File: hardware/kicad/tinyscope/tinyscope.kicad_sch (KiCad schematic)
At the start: 0 parts

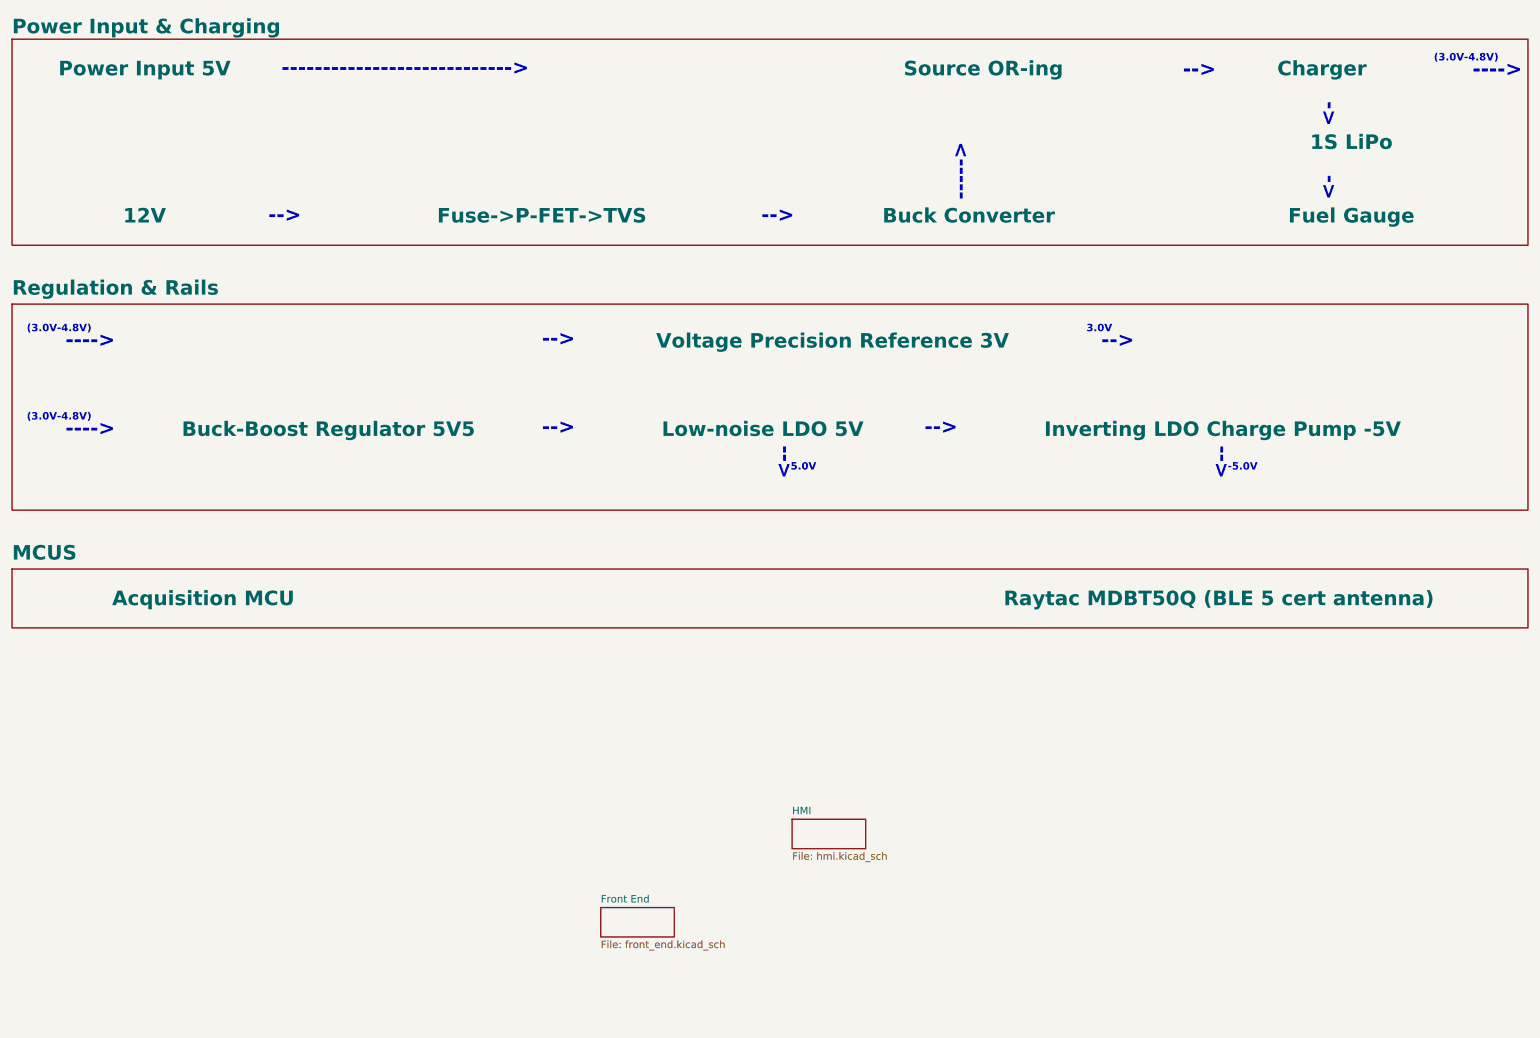
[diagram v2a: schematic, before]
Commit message: feat: hardware: Add tinyscope kicad project. Divide MCU schematic into acquisition and wireless parts
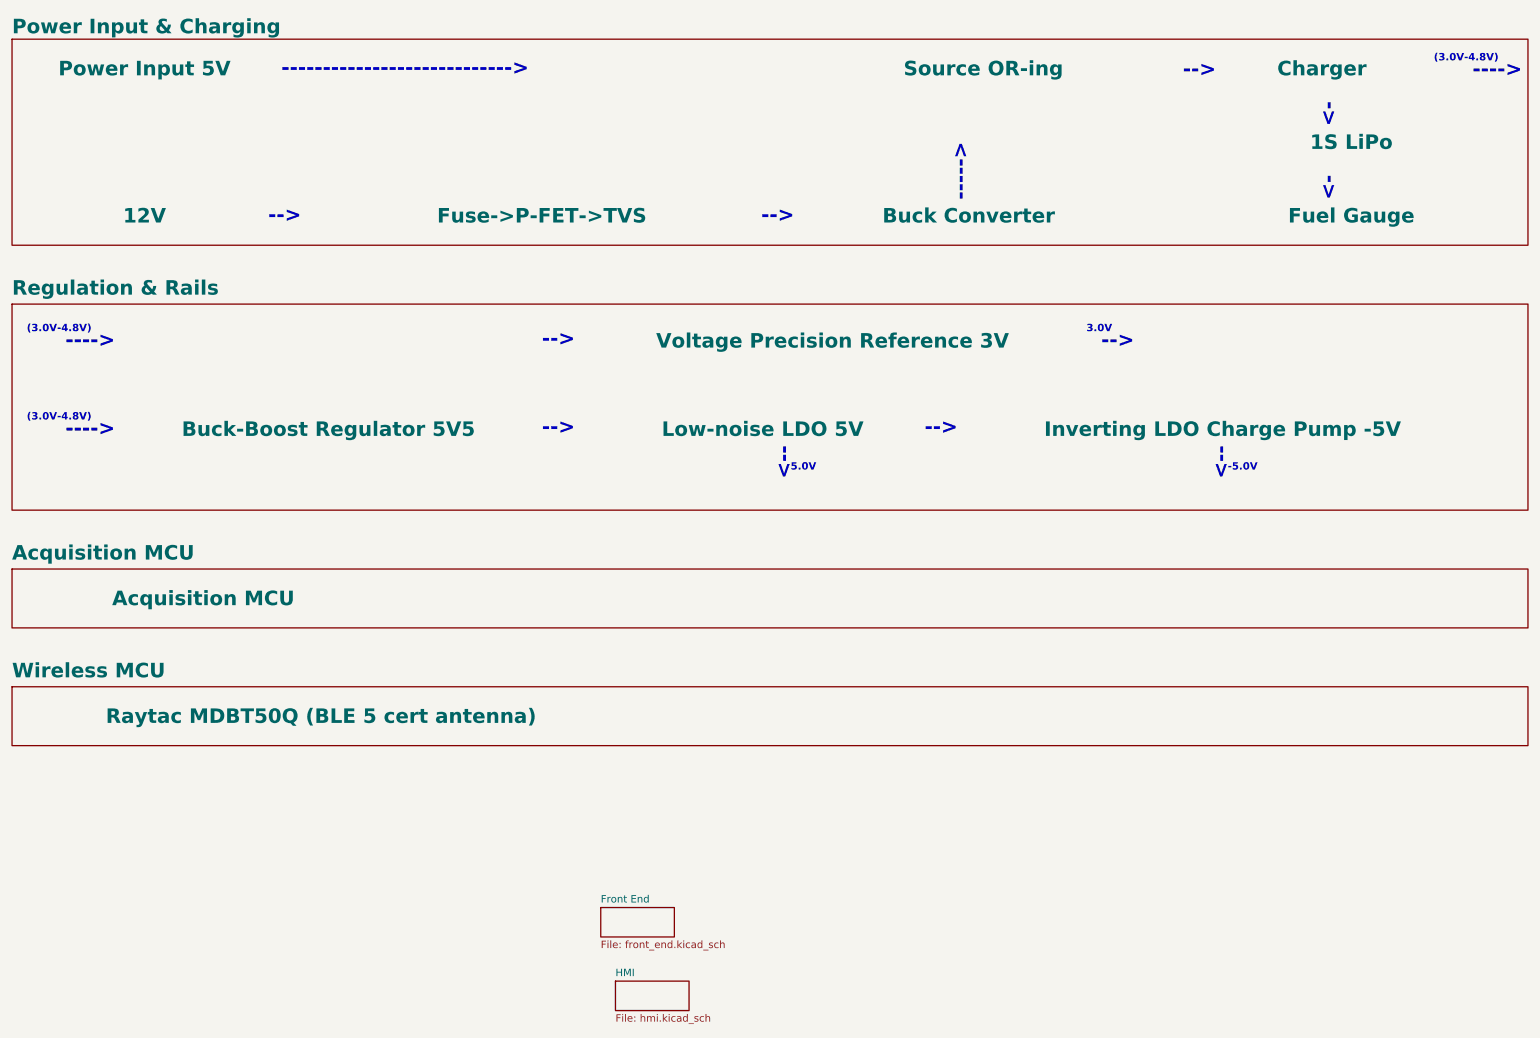
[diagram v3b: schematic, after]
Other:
- sheet MCUS renamed Acquisition MCU
- added sheet Wireless MCU (mcu_wireless.kicad_sch)
- sheet Acquisition MCU: file mcus.kicad_sch -> mcus_acquisition.kicad_sch
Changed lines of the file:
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@@
     )
   )
-  (sheet (at 152.4 154.94) (size 12.7 5.08) (fields_autoplaced)
+  (sheet (at 17.78 132.08) (size 261.62 10.16)
     (stroke (width 0.1524) (type solid))
     (fill (color 255 255 194 1.0000))
-    (property "Sheetname" "HMI" (at 152.4 154.2284 0)
+    (property "Sheetname" "Wireless MCU" (at 17.78 130.7534 0)
+      (effects (font (size 2.5 2.5) bold) (justify left bottom))
+    )
+    (property "Sheetfile" "mcu_wireless.kicad_sch" (at 17.78 142.8246 0)
+      (effects (font (size 1.27 1.27)) (justify left top) hide)
+    )
+    (property "nRF52840" "Raytac MDBT50Q (BLE 5 cert antenna)" (at 71.12 137.16 0) (show_name)
+      (effects (font (size 2.5 2.5) bold))
+    )
+    (instances
+      (project "tinyscope"
+        (path "/bb072e32-cc57-415a-8554-0e84d374f333" (page "7"))
+      )
+    )
+  )
+  (sheet (at 121.92 182.88) (size 12.7 5.08) (fields_autoplaced)
+    (stroke (width 0.1524) (type solid))
+    (fill (color 255 255 194 1.0000))
+    (property "Sheetname" "HMI" (at 121.92 182.1684 0)
       (effects (font (size 1.27 1.27)) (justify left bottom))
     )
-    (property "Sheetfile" "hmi.kicad_sch" (at 152.4 160.6046 0)
+    (property "Sheetfile" "hmi.kicad_sch" (at 121.92 188.5446 0)
       (effects (font (size 1.27 1.27)) (justify left top))
     )
@@
     (stroke (width 0.1524) (type solid))
     (fill (color 255 255 194 1.0000))
-    (property "Sheetname" "MCUS" (at 17.78 110.4334 0)
+    (property "Sheetname" "Acquisition MCU" (at 17.78 110.4334 0)
       (effects (font (size 2.5 2.5) bold) (justify left bottom))
     )
-    (property "Sheetfile" "mcus.kicad_sch" (at 17.78 135.2046 0)
+    (property "Sheetfile" "mcus_acquisition.kicad_sch" (at 17.78 135.2046 0)
       (effects (font (size 1.27 1.27)) (justify left top) hide)
     )
@@
       (effects (font (size 2.5 2.5) bold))
     )
-    (property "nRF52840" "Raytac MDBT50Q (BLE 5 cert antenna)" (at 226.06 116.84 0) (show_name)
-      (effects (font (size 2.5 2.5) bold))
-    )
